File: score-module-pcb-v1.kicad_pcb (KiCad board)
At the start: 4 copper layers, 99.7 x 99.7 mm, 275 parts, among them K1 CONN_3, P1 PINBALL-CONNECTOR, P2 PINBALL-CONNECTOR, P3 SOLENOID-CONNECTOR, P4 CONN_16, P5 CONN_16, P6 HE10-32, Q1 BC846, Q10 DMN6040SSD, Q11 BC846, Q12 BC846, Q13 DMP2240UDM, Q14 DMP2240UDM, Q15 BC846, Q16 BC846, Q17 BC846, Q18 BC846, Q19 DMN6040SSD, Q2 BC846, Q20 DMN6040SSD, Q21 BC846, Q22 BC846, Q23 BC846, Q24 BC846, Q25 BC846, Q26 BC846, Q27 BC846, Q28 BC846, Q29 BSS138, Q3 DMN6040SSD, Q30 FDD5614P, Q31 BC846, Q32 BSS138, Q4 DMN6040SSD, Q5 BC846, Q6 BC846, Q7 BC846, Q8 BC846, Q9 DMN6040SSD, U1 74LVC14, U2 STM32F072R, U3 MCP2562, U4 MC78L05ACH, U5 AP1117IE33G, U6 ZXCT1086E5TA, U7 ZXCT1107SA-7, U8 LM7805CT, U9 MMA8653FC, X1 8.000 MHz

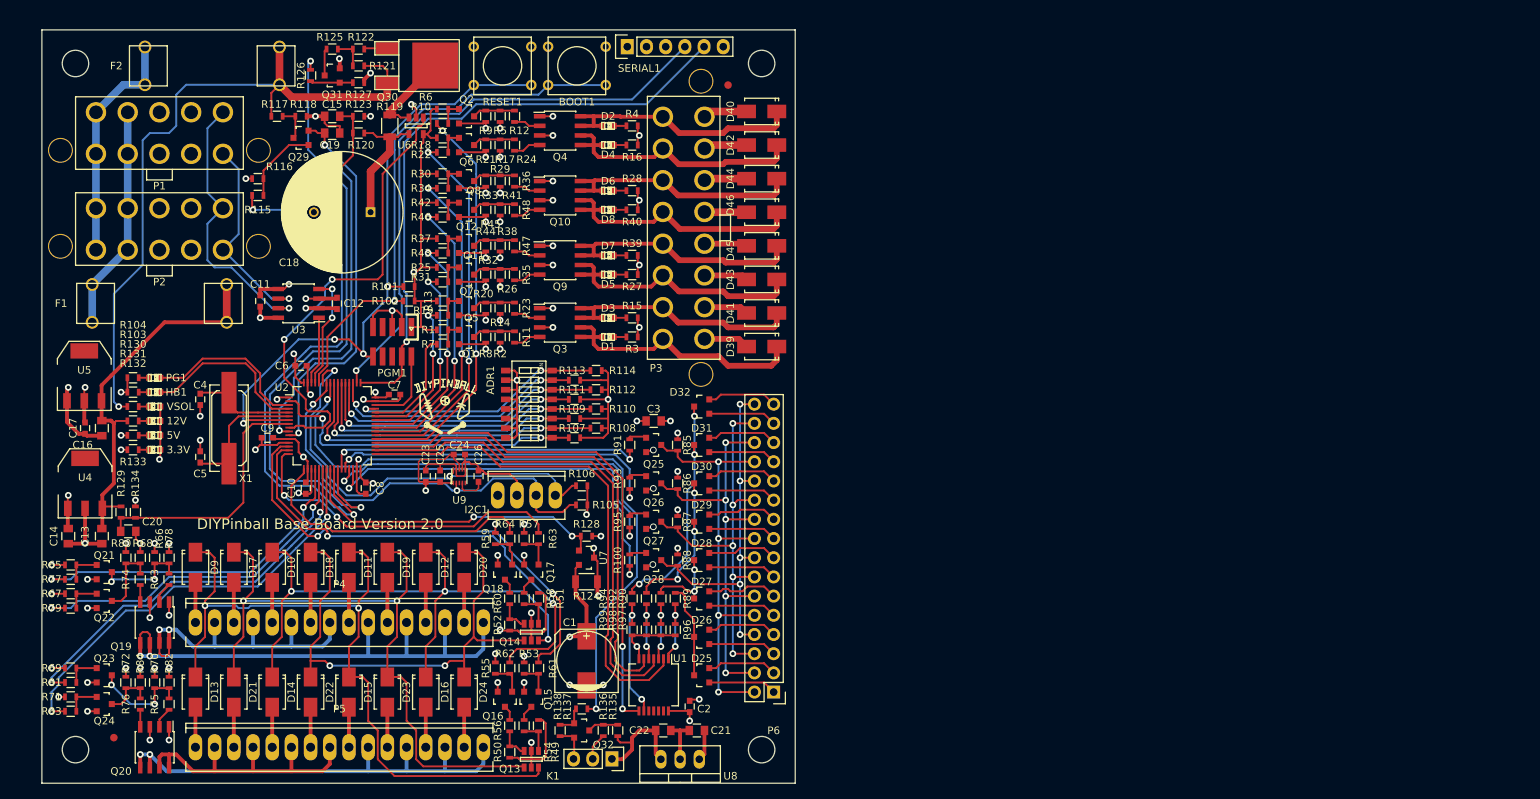
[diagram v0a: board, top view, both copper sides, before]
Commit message: I think the layout is finished now. I'll check again after I sleep.
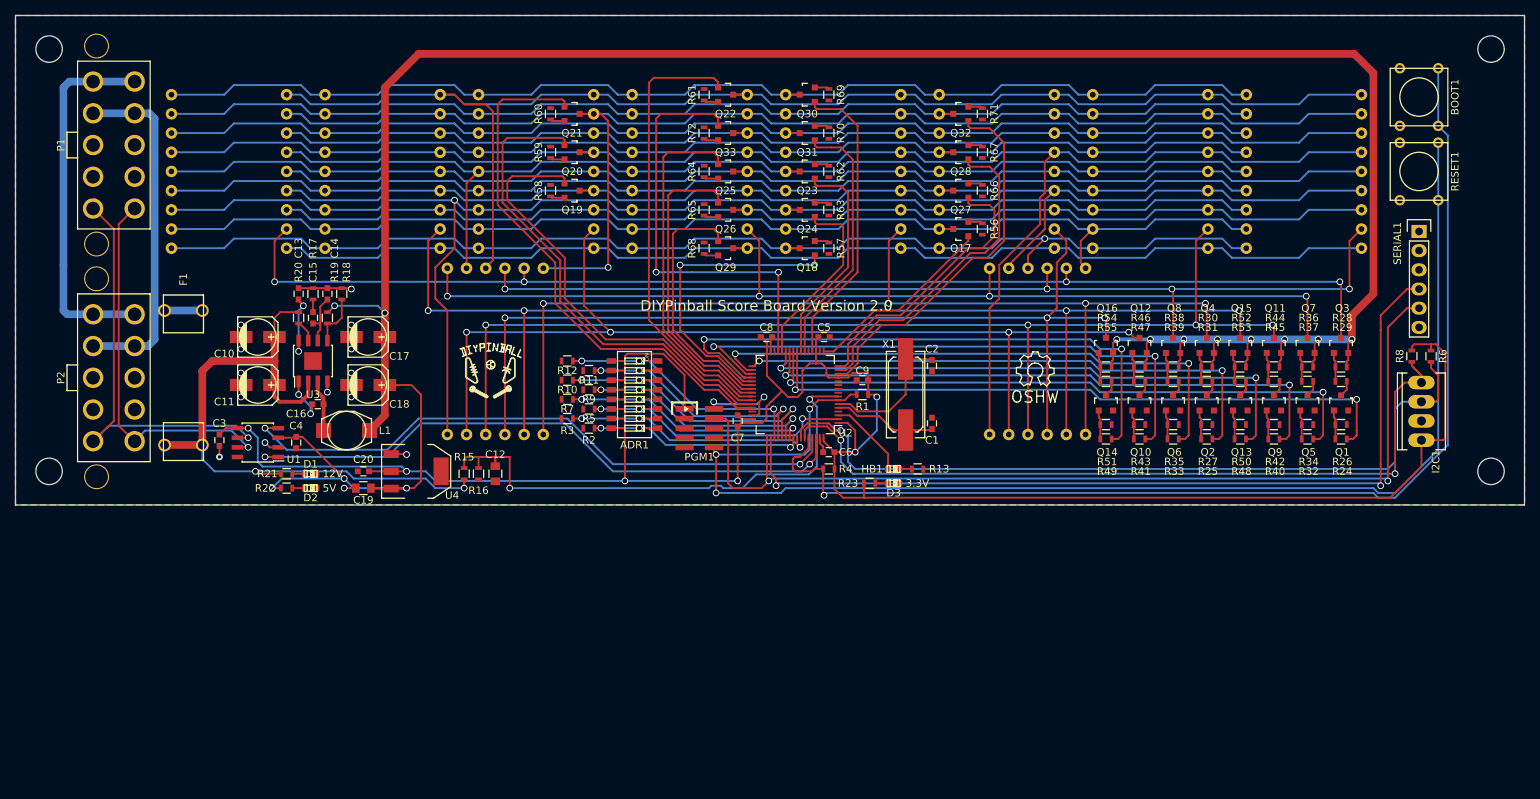
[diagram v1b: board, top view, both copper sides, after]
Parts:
- removed C21, C22: 10u, Capacitors_SMD:C_0805
- removed C23, C24, C26: 100n, Capacitors_SMD:C_0603
- removed C25: 1u, Capacitors_SMD:C_0603
- removed D10, D11, D12, D13, D14, D15, D16, D17, D18, D19, D20, D21, D22, D23, D24, D39, D40, D41, D42, D43, D44, D45, D46, D9: S1M, Diodes_SMD:Diode-SMA_Standard
- removed D25, D26, D27, D28, D29, D30, D31, D32: BAT54C, Housings_SOT-23_SOT-143_TSOT-6:SOT-23
- removed D35, D36, D37, D38, D4, D5, D6, D7, D8, PG1: LED, LEDs:LED-0603
- removed F2: FUSE, PinballParts:FC203-20MM
- removed FIDUCIAL (x2): VAL**, PinballParts:FIDUCIAL
- removed K1: CONN_3, Socket_Strips:Socket_Strip_Straight_1x03
- removed P3: SOLENOID-CONNECTOR, PinballParts:SOLENOID-CONNECTOR-V
- removed P4, P5: CONN_16, PinballParts:Socket_MOLEX-KK-RM2-54mm_Lock_16pin_straight
- removed P6: HE10-32, Pin_Headers:Pin_Header_Straight_2x16
- removed R100, R103, R104, R115, R126, R132, R133, R135, R14, R77, R79, R81, R83, R91, R93, R95: 1K, Resistors_SMD:R_0603
- removed R101, R102, R107, R108, R109, R110, R111, R112, R113, R114, R116, R121, R127, R138, R78, R80, R82, R84, R85, R86, R87, R88, R89, R90, R92, R94, R96, R97, R98, R99: 10K, Resistors_SMD:R_0603
- removed R105, R106: 4.7K, Resistors_SMD:R_0603
- removed R117, R120: 95.3K 1%, Resistors_SMD:R_0603
- removed R118, R123, R128, R134: 5.1K 1%, Resistors_SMD:R_0603
- removed R119: .003, Resistors_SMD:R_1206
- removed R122, R136, R137, R73, R74, R75, R76: 22, Resistors_SMD:R_0603
- removed R124: 0.075, Resistors_SMD:R_1206
- removed R125, R130: 27K, Resistors_SMD:R_0603
- removed R129: 20.5K 1%, Resistors_SMD:R_0603
- removed R131: 2.7K, Resistors_SMD:R_0603
- removed U5: AP1117IE33G, SMD_Packages:SOT-223
- removed U6: ZXCT1086E5TA, Housings_SOT-23_SOT-143_TSOT-6:SOT-23-5
- removed U7: ZXCT1107SA-7, Housings_SOT-23_SOT-143_TSOT-6:SOT-23
- removed U8: LM7805CT, Transistors_TO-220:TO-220_Neutral123_Vertical
- removed U9: MMA8653FC, PinballParts:DFN-10
- added DISP1: 16SEG-1DIGIT-CA, PinballParts:LCSA-8018, B.Cu at (80.6, 98.7)
- added DISP10: 7SEG-4DIGIT-CA, PinballParts:ATA8041, B.Cu at (115.9, 122.6)
- added DISP2: 16SEG-1DIGIT-CA, PinballParts:LCSA-8018, B.Cu at (101.0, 98.7)
- added DISP3: 16SEG-1DIGIT-CA, PinballParts:LCSA-8018, B.Cu at (121.3, 98.7)
- added DISP4: 16SEG-1DIGIT-CA, PinballParts:LCSA-8018, B.Cu at (141.6, 98.7)
- added DISP5: 16SEG-1DIGIT-CA, PinballParts:LCSA-8018, B.Cu at (161.9, 98.7)
- added DISP6: 16SEG-1DIGIT-CA, PinballParts:LCSA-8018, B.Cu at (182.2, 98.7)
- added DISP7: 16SEG-1DIGIT-CA, PinballParts:LCSA-8018, B.Cu at (202.6, 98.7)
- added DISP8: 16SEG-1DIGIT-CA, PinballParts:LCSA-8018, B.Cu at (222.9, 98.7)
- added DISP9: 7SEG-4DIGIT-CA, PinballParts:ATA8041, B.Cu at (187.6, 122.6)
- added L1: 4.7u, Inductors:SELF-WE-PD3S, F.Cu at (96.2, 133.0)
- added Q33: BC846, Housings_SOT-23_SOT-143_TSOT-6:SOT-23, F.Cu at (146.4, 93.7)
- C1: value 47u -> 18p; footprint Capacitors_SMD:c_elec_8x10 -> Capacitors_SMD:C_0603
- C10, C11: value 100n -> 10u; footprint Capacitors_SMD:C_0603 -> Capacitors_SMD:c_elec_5x5.8
- C12: value 100n -> 10u; footprint Capacitors_SMD:C_0603 -> Capacitors_SMD:C_0805
- C13, C3: value 10u -> 100n; footprint Capacitors_SMD:C_0805 -> Capacitors_SMD:C_0603
- C14: value 10u -> NP; footprint Capacitors_SMD:C_0805 -> Capacitors_SMD:C_0603
- C15: value 10u -> 3.3n; footprint Capacitors_SMD:C_0805 -> Capacitors_SMD:C_0603
- C16: value 10u -> 10n; footprint Capacitors_SMD:C_0805 -> Capacitors_SMD:C_0603
- C17: value 4.7u -> 22u; footprint Capacitors_SMD:C_0603 -> Capacitors_SMD:c_elec_5x5.8
- C18: value 470u -> 22u; footprint Capacitors_ThroughHole:C_Radial_D16_L25_P7.5 -> Capacitors_SMD:c_elec_5x5.8
- C2: value 100n -> 18p
- C20: value 10u -> 4.7u; footprint Capacitors_SMD:C_0805 -> Capacitors_SMD:C_0603
- C4: value 18p -> 100n
- C5: value 18p -> 10n
- C8: value 10n -> 100n
- Q10, Q19, Q20, Q9: value DMN6040SSD -> BC846; footprint Housings_SOIC:SOIC-8_3.9x4.9mm_Pitch1.27mm -> Housings_SOT-23_SOT-143_TSOT-6:SOT-23
- Q11, Q12, Q15, Q16, Q7, Q8: value BC846 -> BC856
- Q13, Q14: value DMP2240UDM -> BC846; footprint Housings_SOT-23_SOT-143_TSOT-6:SOT-23-6 -> Housings_SOT-23_SOT-143_TSOT-6:SOT-23
- Q29, Q32: value BSS138 -> BC846
- Q3, Q4: value DMN6040SSD -> BC856; footprint Housings_SOIC:SOIC-8_3.9x4.9mm_Pitch1.27mm -> Housings_SOT-23_SOT-143_TSOT-6:SOT-23
- Q30: value FDD5614P -> BC846; footprint PinballParts:DPAK-2 -> Housings_SOT-23_SOT-143_TSOT-6:SOT-23
- R10, R2, R5, R7: value 1K -> 10K
- R11, R12: value 22 -> 10K
- R13, R25, R32, R33, R49: value 10K -> 1K
- R15: value 2.7K -> 20.5K 1%
- R16: value 2.7K -> 5.1K 1%
- R17: value 1K -> 13K
- R18: value 10K -> 11.8K
- R19: value 1K -> 53.6K
- R21: value 10K -> 2.7K
- R23, R24, R48: value 22 -> 1K
- R26, R34, R38, R43, R46, R54: value 1K -> 4.7K
- R27, R28: value 2.7K -> 4.7K
- R29, R31: value 1K -> 470
- R3, R4: value 2.7K -> 10K
- R30, R42, R44, R50, R51, R52, R6, R8: value 10K -> 4.7K
- R35, R36: value 22 -> 4.7K
- R37, R45, R53, R55: value 10K -> 470
- R39: value 2.7K -> 470
- R40: value 2.7K -> 1K
- R47: value 22 -> 470
- R56, R58, R60, R61, R62, R63, R64, R66, R68, R70, R72: value 1K -> 120
- R57, R59, R65, R67, R69, R71: value 10K -> 120
- REF**: moved to F.Cu
- U1: value 74LVC14 -> MCP2562; footprint Housings_SSOP:SSOP-14_5.3x6.2mm_Pitch0.65mm -> Housings_SOIC:SOIC-8_3.9x4.9mm_Pitch1.27mm
- U3: value MCP2562 -> AP3513E; footprint Housings_SOIC:SOIC-8_3.9x4.9mm_Pitch1.27mm -> Housings_SOIC:SOIC-8-1EP_3.9x4.9mm_Pitch1.27mm
- U4: value MC78L05ACH -> AP1117IE33G
- moved R71 143.2 mm to (180.3, 91.1), turned to 270 degrees
- moved R6 134.8 mm to (239.7, 123.2), turned to 270 degrees
- moved R67 134.0 mm to (180.3, 96.2), turned to 270 degrees
- moved R69 125.8 mm to (160.0, 88.6), turned to 270 degrees
- moved R8 122.6 mm to (237.2, 123.2)
- moved RESET1 122.1 mm to (238.1, 98.7), turned to 90 degrees
- moved R66 119.8 mm to (180.3, 101.3)
- moved I2C1 118.9 mm to (238.4, 130.5), turned to 90 degrees
- moved R34 118.7 mm to (223.4, 132.2)
- moved R24 116.1 mm to (227.8, 134.1), turned to 0 degrees
- moved Q1 116.1 mm to (227.8, 129.4), turned to 0 degrees
- moved R37 116.0 mm to (223.4, 126.5)
- moved R70 115.1 mm to (160.0, 93.7)
- moved Q23 114.5 mm to (157.2, 98.7), turned to 90 degrees
- moved R29 114.4 mm to (227.8, 126.5), turned to 0 degrees
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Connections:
- net /Power Supply/VSOL_IN renamed Net-(P1-Pad1)
- C1 pad 1: /Lamp Driver/LAMP_12V -> Net-(C1-Pad1)
- C10 pad 1: +3.3V -> +12V
- C11 pad 1: +3.3V -> +12V
- C12 pad 1: +5V -> /Control Logic/12V_SENSE
- C13 pad 1: +12V -> Net-(C13-Pad1)
- C14 pad 1: +5V -> Net-(C14-Pad1)
- C15 pad 1: /Control Logic/VSOL_IN_SENSE -> Net-(C14-Pad1)
- C15 pad 2: GND -> Net-(C15-Pad2)
- C16 pad 1: +12V -> Net-(C16-Pad1)
- C16 pad 2: GND -> Net-(C16-Pad2)
- C17 pad 1: +3.3V -> +5V
- C18 pad 1: /Solenoid Driver/SOL_PWR -> +5V
- C19 pad 1: /Control Logic/VSOL_SENSE -> +5V
- C2 pad 1: +3.3V -> Net-(C2-Pad1)
- C20 pad 1: /Control Logic/12V_SENSE -> +3.3V
- C3 pad 1: +12V -> +3.3V
- C4 pad 1: Net-(C4-Pad1) -> +5V
- C5 pad 1: Net-(C5-Pad1) -> +3.3V
- D1 pad 1: Net-(D1-Pad1) -> GND
- D2 pad 1: Net-(D2-Pad1) -> GND
- D3 pad 1: Net-(D3-Pad1) -> GND
- HB1 pad 1: /Control Logic/HEARTBEAT -> Net-(HB1-Pad1)
- HB1 pad 2: Net-(HB1-Pad2) -> /Control Logic/HEARTBEAT
- I2C1 pad 3: /Accelerometer/SCL -> /Control Logic/SCL
- I2C1 pad 4: /Accelerometer/SDA -> /Control Logic/SDA
- Q10 pad 1: GND -> Net-(Q10-Pad1)
- Q10 pad 2: Net-(Q10-Pad2) -> GND
- Q10 pad 3: GND -> Net-(Q10-Pad3)
- Q11 pad 2: GND -> +5V
- Q11 pad 3: Net-(Q11-Pad3) -> /16-Segment Digits/ANODE2
- Q12 pad 2: GND -> +5V
- Q12 pad 3: Net-(Q12-Pad3) -> /16-Segment Digits/ANODE6
- Q13 pad 2: /Lamp Driver/LAMP_12V -> GND
- Q14 pad 2: /Lamp Driver/LAMP_12V -> GND
- Q15 pad 2: GND -> +5V
- Q15 pad 3: Net-(Q15-Pad3) -> /16-Segment Digits/ANODE3
- Q16 pad 2: GND -> +5V
- Q16 pad 3: Net-(Q16-Pad3) -> /16-Segment Digits/ANODE7
- Q17 pad 1: Net-(Q17-Pad1) -> /Cathode Driver/CATHODE0
- Q17 pad 2: GND -> Net-(Q17-Pad2)
- Q17 pad 3: Net-(Q17-Pad3) -> /16-Segment Digits/CATHODE0
- Q18 pad 1: Net-(Q18-Pad1) -> /Cathode Driver/CATHODE1
- Q18 pad 2: GND -> Net-(Q18-Pad2)
- Q18 pad 3: Net-(Q18-Pad3) -> /16-Segment Digits/CATHODE1
- Q19 pad 1: GND -> /Cathode Driver/CATHODE2
- Q19 pad 3: GND -> /16-Segment Digits/CATHODE2
- Q20 pad 1: GND -> /Cathode Driver/CATHODE3
- Q20 pad 3: GND -> /16-Segment Digits/CATHODE3
- Q21 pad 1: Net-(Q21-Pad1) -> /Cathode Driver/CATHODE4
- Q21 pad 2: GND -> Net-(Q21-Pad2)
- Q21 pad 3: Net-(Q21-Pad3) -> /16-Segment Digits/CATHODE4
- Q22 pad 1: Net-(Q22-Pad1) -> /Cathode Driver/CATHODE5
- Q22 pad 2: GND -> Net-(Q22-Pad2)
- Q22 pad 3: Net-(Q22-Pad3) -> /16-Segment Digits/CATHODE5
- Q23 pad 1: Net-(Q23-Pad1) -> /Cathode Driver/CATHODE6
- Q23 pad 2: GND -> Net-(Q23-Pad2)
- Q23 pad 3: Net-(Q23-Pad3) -> /16-Segment Digits/CATHODE6
- Q24 pad 1: Net-(Q24-Pad1) -> /Cathode Driver/CATHODE7
- Q24 pad 2: GND -> Net-(Q24-Pad2)
- Q24 pad 3: Net-(Q24-Pad3) -> /16-Segment Digits/CATHODE7
- Q25 pad 1: Net-(Q25-Pad1) -> /Cathode Driver/CATHODE8
- Q25 pad 2: GND -> Net-(Q25-Pad2)
- Q25 pad 3: /Switch Matrix/COL0_SWITCHED -> /16-Segment Digits/CATHODE8
- Q26 pad 1: Net-(Q26-Pad1) -> /Cathode Driver/CATHODE9
- Q26 pad 2: GND -> Net-(Q26-Pad2)
- Q26 pad 3: /Switch Matrix/COL1_SWITCHED -> /16-Segment Digits/CATHODE9
- Q27 pad 1: Net-(Q27-Pad1) -> /Cathode Driver/CATHODE10
- Q27 pad 2: GND -> Net-(Q27-Pad2)
- Q27 pad 3: /Switch Matrix/COL2_SWITCHED -> /16-Segment Digits/CATHODE10
- Q28 pad 1: Net-(Q28-Pad1) -> /Cathode Driver/CATHODE11
- Q28 pad 2: GND -> Net-(Q28-Pad2)
- Q28 pad 3: /Switch Matrix/COL3_SWITCHED -> /16-Segment Digits/CATHODE11
- Q29 pad 1: Net-(Q29-Pad1) -> /Cathode Driver/CATHODE12
- Q29 pad 2: /Control Logic/VSOL_IN_SENSE -> Net-(Q29-Pad2)
- Q29 pad 3: Net-(Q29-Pad3) -> /16-Segment Digits/CATHODE12
- Q3 pad 1: GND -> Net-(Q3-Pad1)
- Q3 pad 2: Net-(Q3-Pad2) -> +5V
- Q3 pad 3: GND -> /16-Segment Digits/ANODE0
- Q31 pad 1: Net-(Q31-Pad1) -> /Cathode Driver/CATHODE14
- Q31 pad 2: GND -> Net-(Q31-Pad2)
- Q31 pad 3: Net-(Q31-Pad3) -> /16-Segment Digits/CATHODE14
- Q32 pad 1: Net-(Q32-Pad1) -> /Cathode Driver/CATHODE15
- Q32 pad 2: GND -> Net-(Q32-Pad2)
- Q32 pad 3: Net-(Q32-Pad3) -> /16-Segment Digits/CATHODE15
- Q4 pad 1: GND -> Net-(Q4-Pad1)
- Q4 pad 2: Net-(Q4-Pad2) -> +5V
- Q4 pad 3: GND -> /16-Segment Digits/ANODE4
- Q7 pad 2: GND -> +5V
- Q7 pad 3: Net-(Q7-Pad3) -> /16-Segment Digits/ANODE1
- Q8 pad 2: GND -> +5V
- Q8 pad 3: Net-(Q8-Pad3) -> /16-Segment Digits/ANODE5
- Q9 pad 1: GND -> Net-(Q9-Pad1)
- Q9 pad 2: Net-(Q9-Pad2) -> GND
- Q9 pad 3: GND -> Net-(Q9-Pad3)
- R1 pad 2: Net-(Q1-Pad1) -> /Control Logic/~RESET
- R10 pad 1: /Control Logic/SOLENOID7 -> /Control Logic/ADDRESS2
- R10 pad 2: Net-(Q2-Pad1) -> GND
- R11 pad 1: Net-(Q3-Pad4) -> /Control Logic/ADDRESS1
- R11 pad 2: Net-(Q1-Pad3) -> GND
- R12 pad 1: Net-(Q2-Pad3) -> /Control Logic/ADDRESS0
- R12 pad 2: Net-(Q4-Pad2) -> GND
- R13 pad 1: +3.3V -> Net-(HB1-Pad1)
- R13 pad 2: Net-(Q5-Pad1) -> GND
- R15 pad 1: +12V -> /Control Logic/12V_SENSE
- R15 pad 2: Net-(D3-Pad1) -> +12V
- R16 pad 1: +12V -> /Control Logic/12V_SENSE
- R16 pad 2: Net-(D4-Pad1) -> GND
- R17 pad 1: +12V -> GND
- R17 pad 2: Net-(Q6-Pad3) -> Net-(C15-Pad2)
- R18 pad 1: +3.3V -> GND
- R18 pad 2: Net-(Q6-Pad1) -> Net-(R18-Pad2)
- R19 pad 1: /Control Logic/SOLENOID1 -> Net-(R18-Pad2)
- R19 pad 2: Net-(Q5-Pad1) -> +5V
- R2 pad 1: +12V -> /Control Logic/ADDRESS7
- R2 pad 2: Net-(Q1-Pad3) -> GND
- R20 pad 1: Net-(Q5-Pad3) -> Net-(R20-Pad1)
- R20 pad 2: GND -> +12V
- R21 pad 1: Net-(Q6-Pad3) -> +12V
- R21 pad 2: GND -> Net-(D1-Pad2)
- R22 pad 1: /Control Logic/SOLENOID6 -> +5V
- R22 pad 2: Net-(Q6-Pad1) -> Net-(D2-Pad2)
- R23 pad 1: Net-(Q3-Pad2) -> +3.3V
- R23 pad 2: Net-(Q5-Pad3) -> Net-(D3-Pad2)
- R24 pad 1: Net-(Q6-Pad3) -> Net-(Q1-Pad1)
- R24 pad 2: Net-(Q4-Pad4) -> /Anode Driver/ANODE0
- R25 pad 1: +3.3V -> Net-(Q2-Pad1)
- R25 pad 2: Net-(Q7-Pad1) -> /Anode Driver/ANODE4
- R26 pad 1: +12V -> Net-(Q1-Pad1)
- R26 pad 2: Net-(Q7-Pad3) -> GND
- R27 pad 1: +12V -> Net-(Q2-Pad1)
- R27 pad 2: Net-(D5-Pad1) -> GND
- R28 pad 1: +12V -> +5V
- R28 pad 2: Net-(D6-Pad1) -> Net-(Q3-Pad1)
- R29 pad 1: +12V -> Net-(Q3-Pad1)
- R29 pad 2: Net-(Q8-Pad3) -> Net-(Q1-Pad3)
- R3 pad 1: +12V -> /Control Logic/ADDRESS6
- R3 pad 2: Net-(D1-Pad1) -> GND
- R30 pad 1: +3.3V -> +5V
- R30 pad 2: Net-(Q8-Pad1) -> Net-(Q4-Pad1)
- R31 pad 1: /Control Logic/SOLENOID2 -> Net-(Q4-Pad1)
- R31 pad 2: Net-(Q7-Pad1) -> Net-(Q2-Pad3)
- R32 pad 1: Net-(Q7-Pad3) -> Net-(Q5-Pad1)
- R32 pad 2: GND -> /Anode Driver/ANODE1
- R33 pad 1: Net-(Q8-Pad3) -> Net-(Q6-Pad1)
- R33 pad 2: GND -> /Anode Driver/ANODE5
- R34 pad 1: /Control Logic/SOLENOID5 -> Net-(Q5-Pad1)
- R34 pad 2: Net-(Q8-Pad1) -> GND
- R35 pad 1: Net-(Q9-Pad4) -> Net-(Q6-Pad1)
- R35 pad 2: Net-(Q7-Pad3) -> GND
- R36 pad 1: Net-(Q8-Pad3) -> +5V
- R36 pad 2: Net-(Q10-Pad2) -> Net-(Q7-Pad1)
- R37 pad 1: +3.3V -> Net-(Q7-Pad1)
- R37 pad 2: Net-(Q11-Pad1) -> Net-(Q5-Pad3)
- R38 pad 1: +12V -> +5V
- R38 pad 2: Net-(Q11-Pad3) -> Net-(Q8-Pad1)
- R39 pad 1: +12V -> Net-(Q8-Pad1)
- R39 pad 2: Net-(D7-Pad1) -> Net-(Q6-Pad3)
- R4 pad 1: +12V -> +3.3V
- R4 pad 2: Net-(D2-Pad1) -> /Control Logic/BOOTLOADER
- R40 pad 1: +12V -> Net-(Q9-Pad1)
- R40 pad 2: Net-(D8-Pad1) -> /Anode Driver/ANODE2
- R41 pad 1: +12V -> Net-(Q10-Pad1)
- R41 pad 2: Net-(Q12-Pad3) -> /Anode Driver/ANODE6
- R42 pad 1: +3.3V -> Net-(Q9-Pad1)
- R42 pad 2: Net-(Q12-Pad1) -> GND
- R43 pad 1: /Control Logic/SOLENOID3 -> Net-(Q10-Pad1)
- R43 pad 2: Net-(Q11-Pad1) -> GND
- R44 pad 1: Net-(Q11-Pad3) -> +5V
- R44 pad 2: GND -> Net-(Q11-Pad1)
- R45 pad 1: Net-(Q12-Pad3) -> Net-(Q11-Pad1)
- R45 pad 2: GND -> Net-(Q9-Pad3)
- R46 pad 1: /Control Logic/SOLENOID4 -> +5V
- R47 pad 1: Net-(Q9-Pad2) -> Net-(Q12-Pad1)
- R47 pad 2: Net-(Q11-Pad3) -> Net-(Q10-Pad3)
- R48 pad 1: Net-(Q12-Pad3) -> Net-(Q13-Pad1)
- R48 pad 2: Net-(Q10-Pad4) -> /Anode Driver/ANODE3
- R49 pad 1: /Lamp Driver/LAMP_12V -> Net-(Q14-Pad1)
- R49 pad 2: Net-(Q13-Pad1) -> /Anode Driver/ANODE7
- R5 pad 1: +12V -> /Control Logic/ADDRESS5
- R5 pad 2: Net-(Q2-Pad3) -> GND
- R50 pad 1: /Lamp Driver/LAMP_12V -> Net-(Q13-Pad1)
- R50 pad 2: Net-(Q13-Pad3) -> GND
- R51 pad 1: /Lamp Driver/LAMP_12V -> Net-(Q14-Pad1)
- R51 pad 2: Net-(Q14-Pad1) -> GND
- R52 pad 1: /Lamp Driver/LAMP_12V -> +5V
- R52 pad 2: Net-(Q14-Pad3) -> Net-(Q15-Pad1)
- R53 pad 1: GND -> Net-(Q15-Pad1)
- R53 pad 2: Net-(Q15-Pad1) -> Net-(Q13-Pad3)
- R54 pad 1: Net-(Q13-Pad1) -> +5V
- R54 pad 2: Net-(Q15-Pad3) -> Net-(Q16-Pad1)
- R55 pad 1: GND -> Net-(Q16-Pad1)
- R55 pad 2: Net-(Q16-Pad1) -> Net-(Q14-Pad3)
- R56 pad 1: Net-(Q13-Pad3) -> Net-(Q17-Pad2)
- R56 pad 2: Net-(Q16-Pad3) -> GND
- R57 pad 1: GND -> Net-(Q18-Pad2)
- R57 pad 2: Net-(Q17-Pad1) -> GND
- R58 pad 1: Net-(Q14-Pad1) -> Net-(Q19-Pad2)
- R58 pad 2: Net-(Q17-Pad3) -> GND
- R59 pad 1: GND -> Net-(Q20-Pad2)
- R59 pad 2: Net-(Q18-Pad1) -> GND
- R6 pad 2: Net-(Q2-Pad1) -> /Control Logic/SCL
- R60 pad 1: Net-(Q14-Pad3) -> Net-(Q21-Pad2)
- R60 pad 2: Net-(Q18-Pad3) -> GND
- R61 pad 1: /Control Logic/LAMP_ROW0 -> Net-(Q22-Pad2)
- R61 pad 2: Net-(Q15-Pad1) -> GND
- R62 pad 1: /Control Logic/LAMP_ROW1 -> Net-(Q23-Pad2)
- R62 pad 2: Net-(Q16-Pad1) -> GND
- R63 pad 1: /Control Logic/LAMP_ROW2 -> Net-(Q24-Pad2)
- R63 pad 2: Net-(Q17-Pad1) -> GND
- R64 pad 1: /Control Logic/LAMP_ROW3 -> Net-(Q25-Pad2)
- R64 pad 2: Net-(Q18-Pad1) -> GND
- R65 pad 1: +3.3V -> Net-(Q26-Pad2)
- R65 pad 2: Net-(Q21-Pad1) -> GND
- R66 pad 1: /Lamp Driver/LAMP_12V -> Net-(Q27-Pad2)
- R66 pad 2: Net-(Q21-Pad3) -> GND
- R67 pad 1: +3.3V -> Net-(Q28-Pad2)
- R67 pad 2: Net-(Q22-Pad1) -> GND
- R68 pad 1: /Lamp Driver/LAMP_12V -> Net-(Q29-Pad2)
- R68 pad 2: Net-(Q22-Pad3) -> GND
- R69 pad 1: +3.3V -> Net-(Q30-Pad2)
- R69 pad 2: Net-(Q23-Pad1) -> GND
- R7 pad 1: /Control Logic/SOLENOID0 -> /Control Logic/ADDRESS4
- R7 pad 2: Net-(Q1-Pad1) -> GND
- R70 pad 1: /Lamp Driver/LAMP_12V -> Net-(Q31-Pad2)
- R70 pad 2: Net-(Q23-Pad3) -> GND
- R71 pad 1: +3.3V -> Net-(Q32-Pad2)
- R71 pad 2: Net-(Q24-Pad1) -> GND
- R72 pad 1: /Lamp Driver/LAMP_12V -> Net-(Q33-Pad2)
- R72 pad 2: Net-(Q24-Pad3) -> GND
- R8 pad 1: Net-(Q1-Pad3) -> +3.3V
- R8 pad 2: GND -> /Control Logic/SDA
- R9 pad 1: Net-(Q2-Pad3) -> /Control Logic/ADDRESS3
- U1 pad 1: Net-(R89-Pad1) -> /Control Logic/CANTX
- U1 pad 2: /Switch Matrix/ROW0 -> GND
- U1 pad 3: Net-(R90-Pad1) -> +5V
- U1 pad 4: /Switch Matrix/ROW1 -> /Control Logic/CANRX
- U1 pad 5: Net-(R92-Pad1) -> +3.3V
- U1 pad 6: /Switch Matrix/ROW2 -> /Control Logic/CANL
- U1 pad 7: GND -> /Control Logic/CANH
- U1 pad 8: /Switch Matrix/ROW3 -> GND
- U2 pad 10: /Control Logic/VSOL_SENSE -> (no net)
- U2 pad 11: /Control Logic/VSOL_IN_SENSE -> (no net)
- U2 pad 14: /Control Logic/LAMP_ROW0 -> /Cathode Driver/CATHODE15
- U2 pad 15: /Control Logic/LAMP_ROW1 -> /Cathode Driver/CATHODE11
- U2 pad 16: /Control Logic/LAMP_ROW2 -> /Cathode Driver/CATHODE10
- U2 pad 17: /Control Logic/LAMP_ROW3 -> /Cathode Driver/CATHODE0
- U2 pad 2: /Control Logic/ADDRESS7 -> /Control Logic/ADDRESS5
- U2 pad 20: /Control Logic/LAMP_COL0 -> /Cathode Driver/CATHODE13
- U2 pad 21: /Control Logic/LAMP_COL1 -> (no net)
- U2 pad 22: /Control Logic/LAMP_COL2 -> /Cathode Driver/CATHODE14
- U2 pad 23: /Control Logic/LAMP_COL3 -> /Cathode Driver/CATHODE6
- U2 pad 24: /Power Supply/ILAMP_SENSE_OUT -> /Anode Driver/ANODE0
- U2 pad 25: /Control Logic/VSOL_MEASURE_CONTROL -> /Anode Driver/ANODE1
- U2 pad 26: /Control Logic/VSOL_PRECHARGE_PWM -> /Anode Driver/ANODE2
- U2 pad 27: /Switch Matrix/COL0 -> /Anode Driver/ANODE3
- U2 pad 28: /Switch Matrix/COL1 -> /Cathode Driver/CATHODE7
- U2 pad 29: /Switch Matrix/COL2 -> /Cathode Driver/CATHODE16
- U2 pad 3: /Control Logic/POWER_GOOD -> /Control Logic/HEARTBEAT
- U2 pad 30: /Switch Matrix/COL3 -> (no net)
- U2 pad 33: /Switch Matrix/ROW0 -> /Anode Driver/ANODE4
- U2 pad 34: /Switch Matrix/ROW1 -> /Anode Driver/ANODE5
- U2 pad 35: /Switch Matrix/ROW2 -> /Anode Driver/ANODE6
- U2 pad 36: /Switch Matrix/ROW3 -> /Anode Driver/ANODE7
- U2 pad 37: /Control Logic/SOLENOID7 -> /Cathode Driver/CATHODE1
- U2 pad 38: /Control Logic/SOLENOID6 -> /Cathode Driver/CATHODE12
- U2 pad 39: /Control Logic/SOLENOID5 -> /Cathode Driver/CATHODE9
- U2 pad 4: /Control Logic/HEARTBEAT -> (no net)
- U2 pad 40: /Control Logic/SOLENOID4 -> /Cathode Driver/CATHODE8
- U2 pad 41: /Control Logic/SOLENOID3 -> /Cathode Driver/CATHODE5
- U2 pad 42: /Control Logic/SOLENOID2 -> /Cathode Driver/CATHODE2
- U2 pad 43: /Control Logic/SOLENOID1 -> /Cathode Driver/CATHODE3
- U2 pad 44: /Control Logic/SOLENOID0 -> /Cathode Driver/CATHODE4
- U2 pad 45: /Control Logic/ADDRESS0 -> (no net)
- U2 pad 5: Net-(C4-Pad1) -> Net-(C1-Pad1)
- U2 pad 51: /Control Logic/ADDRESS1 -> /Control Logic/ADDRESS0
- U2 pad 52: /Control Logic/ADDRESS2 -> /Control Logic/ADDRESS1
- U2 pad 53: /Control Logic/ADDRESS3 -> /Control Logic/ADDRESS2
- U2 pad 54: /Control Logic/ADDRESS4 -> /Control Logic/ADDRESS3
- U2 pad 55: /Control Logic/ADDRESS5 -> /Control Logic/ADDRESS4
- U2 pad 56: /Control Logic/ADDRESS6 -> /Control Logic/ADDRESS7
- U2 pad 57: /RGB LED Output/RGB_DATA -> /Control Logic/ADDRESS6
- U2 pad 58: /Accelerometer/SCL -> /Control Logic/SCL
- U2 pad 59: /Accelerometer/SDA -> /Control Logic/SDA
- U2 pad 6: Net-(C5-Pad1) -> Net-(C2-Pad1)
- U2 pad 9: /Power Supply/ISOL_SENSE_OUT -> (no net)
- U3 pad 1: /Control Logic/CANTX -> Net-(C16-Pad2)
- U3 pad 2: GND -> +12V
- U3 pad 3: +5V -> Net-(C16-Pad1)
- U3 pad 4: /Control Logic/CANRX -> GND
- U3 pad 5: +3.3V -> Net-(R18-Pad2)
- U3 pad 6: /Control Logic/CANL -> Net-(C14-Pad1)
- U3 pad 7: /Control Logic/CANH -> Net-(R20-Pad1)
- U3 pad 8: GND -> Net-(C13-Pad1)
- U4 pad 1: +5V -> GND
- U4 pad 2: GND -> +3.3V
- U4 pad 3: +12V -> +5V
- X1 pad 1: Net-(C4-Pad1) -> Net-(C1-Pad1)
- X1 pad 2: Net-(C5-Pad1) -> Net-(C2-Pad1)
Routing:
- net +5V: track 66.0 -> 342.2 mm, vias 3 -> 13
- net GND: track 248.1 -> 34.7 mm, vias 67 -> 14
- net /16-Segment Digits/CATHODE3: track 0.00 -> 192.4 mm
- net /16-Segment Digits/CATHODE7: track 0.00 -> 184.2 mm, vias 0 -> 1
- net /16-Segment Digits/CATHODE4: track 0.00 -> 181.8 mm, vias 0 -> 1
- net /16-Segment Digits/CATHODE5: track 0.00 -> 180.5 mm
- net /16-Segment Digits/CATHODE6: track 0.00 -> 164.9 mm
- net /16-Segment Digits/CATHODE2: track 0.00 -> 164.2 mm
- net /16-Segment Digits/ANODE0: track 0.00 -> 160.3 mm, vias 0 -> 4
- net /16-Segment Digits/CATHODE0: track 0.00 -> 157.6 mm
- net /16-Segment Digits/CATHODE1: track 0.00 -> 156.3 mm, vias 0 -> 1
- net /16-Segment Digits/ANODE3: track 0.00 -> 155.2 mm, vias 0 -> 4
- net /16-Segment Digits/CATHODE16: track 0.00 -> 151.5 mm
- net /16-Segment Digits/CATHODE9: track 0.00 -> 151.5 mm
- net /16-Segment Digits/CATHODE10: track 0.00 -> 151.5 mm
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- added copper zone on B.Cu, net GND
- added copper zone on F.Cu, net GND
- removed copper zone on Power.Cu, net +12V
- removed copper zone on Power.Cu, net +3.3V
- removed copper zone on Power.Cu, net /Lamp Driver/LAMP_12V
- removed copper zone on Power.Cu, net /Solenoid Driver/SOL_PWR
- removed copper zone on Ground.Cu, net GND
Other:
- board size 99.7 x 99.7 mm -> 199.7 x 64.8 mm
- board text added: "DIYPinball Score Board Version 2.0"
- board text removed: "DIYPinball Base Board Version 2.0"
- board text removed: "VSOL"
